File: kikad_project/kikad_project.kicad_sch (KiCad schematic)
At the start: 33 parts, among them IC1 HCPL-2531, IC2 HCPL-2531, IC3 HCPL-2531, M1 Motor_DC, M2 Motor_DC, M3 Motor_DC, M4 Stepper_Motor_bipolar, Q2 IRF5305PbF, SW1 SW_Push, U1 NRF24L01_Breakout, U10 TCST2103_MODULE, U11 DM556T, U2 STM32F103C8T6, U3 L7805, U4 L7805, U5 MD13S, U6 MD13S, U7 MD13S, U8 TCST2103_MODULE, U9 TCST2103_MODULE

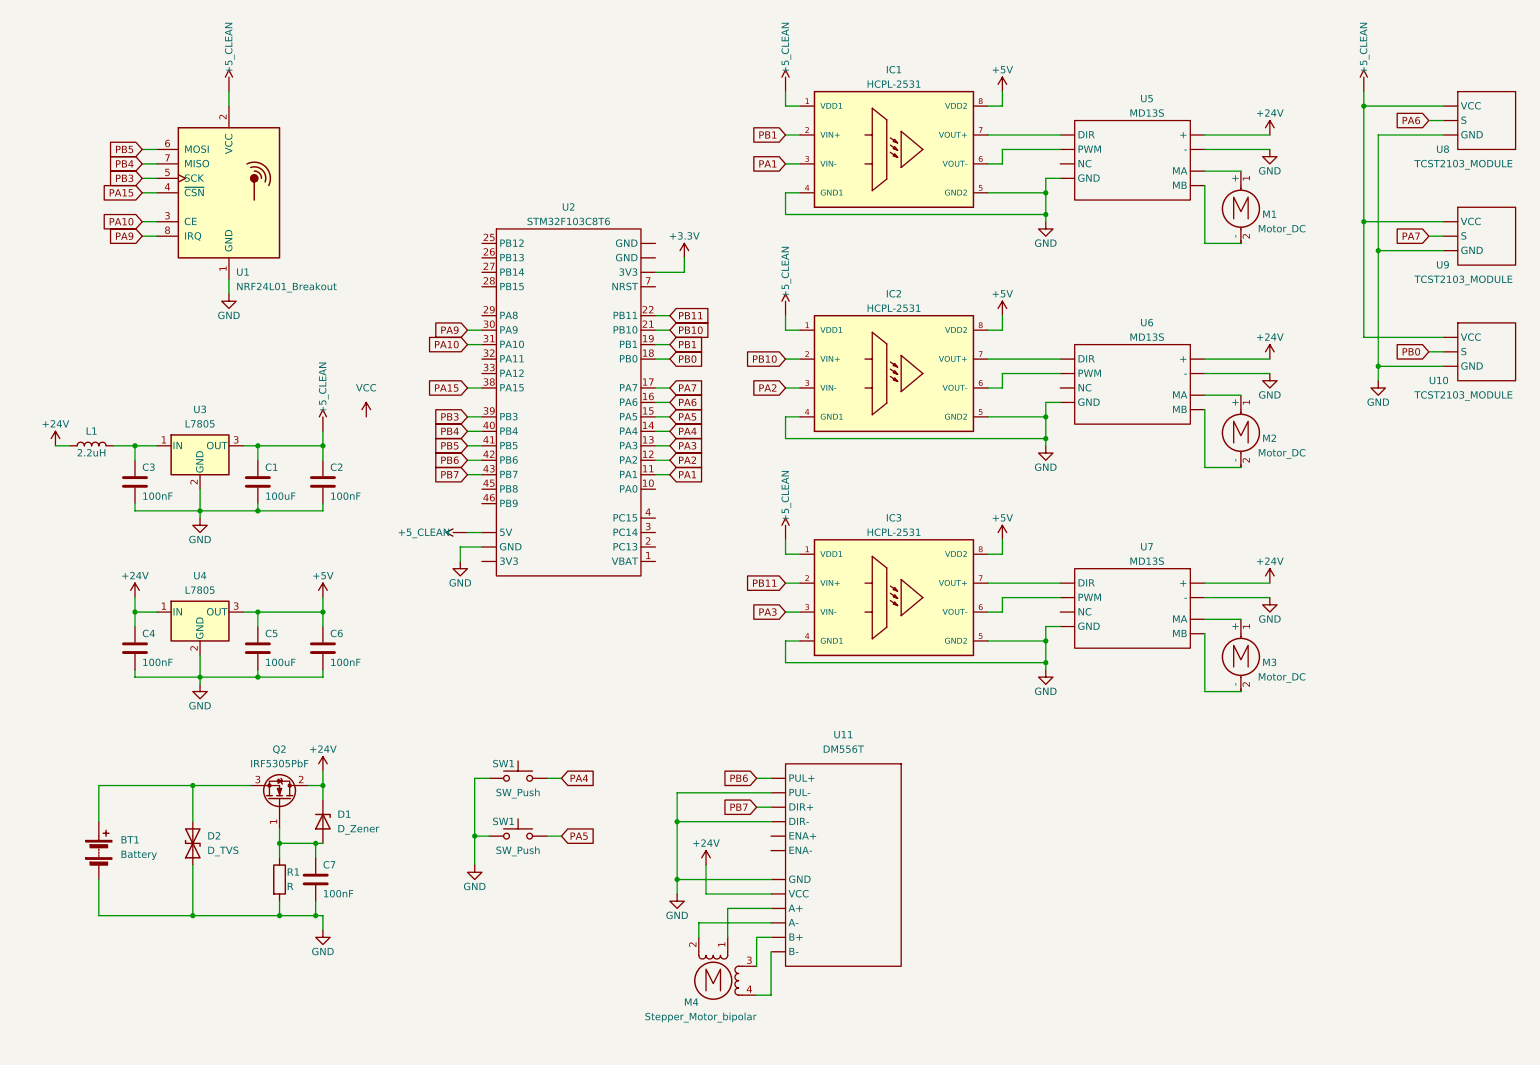
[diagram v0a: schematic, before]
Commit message: Schematics ready(excluding PCB design)
The electric schema for the PCB in the robot and the mounting schema are ready. The footprints for each element are present. However, the PCB design is not ready.
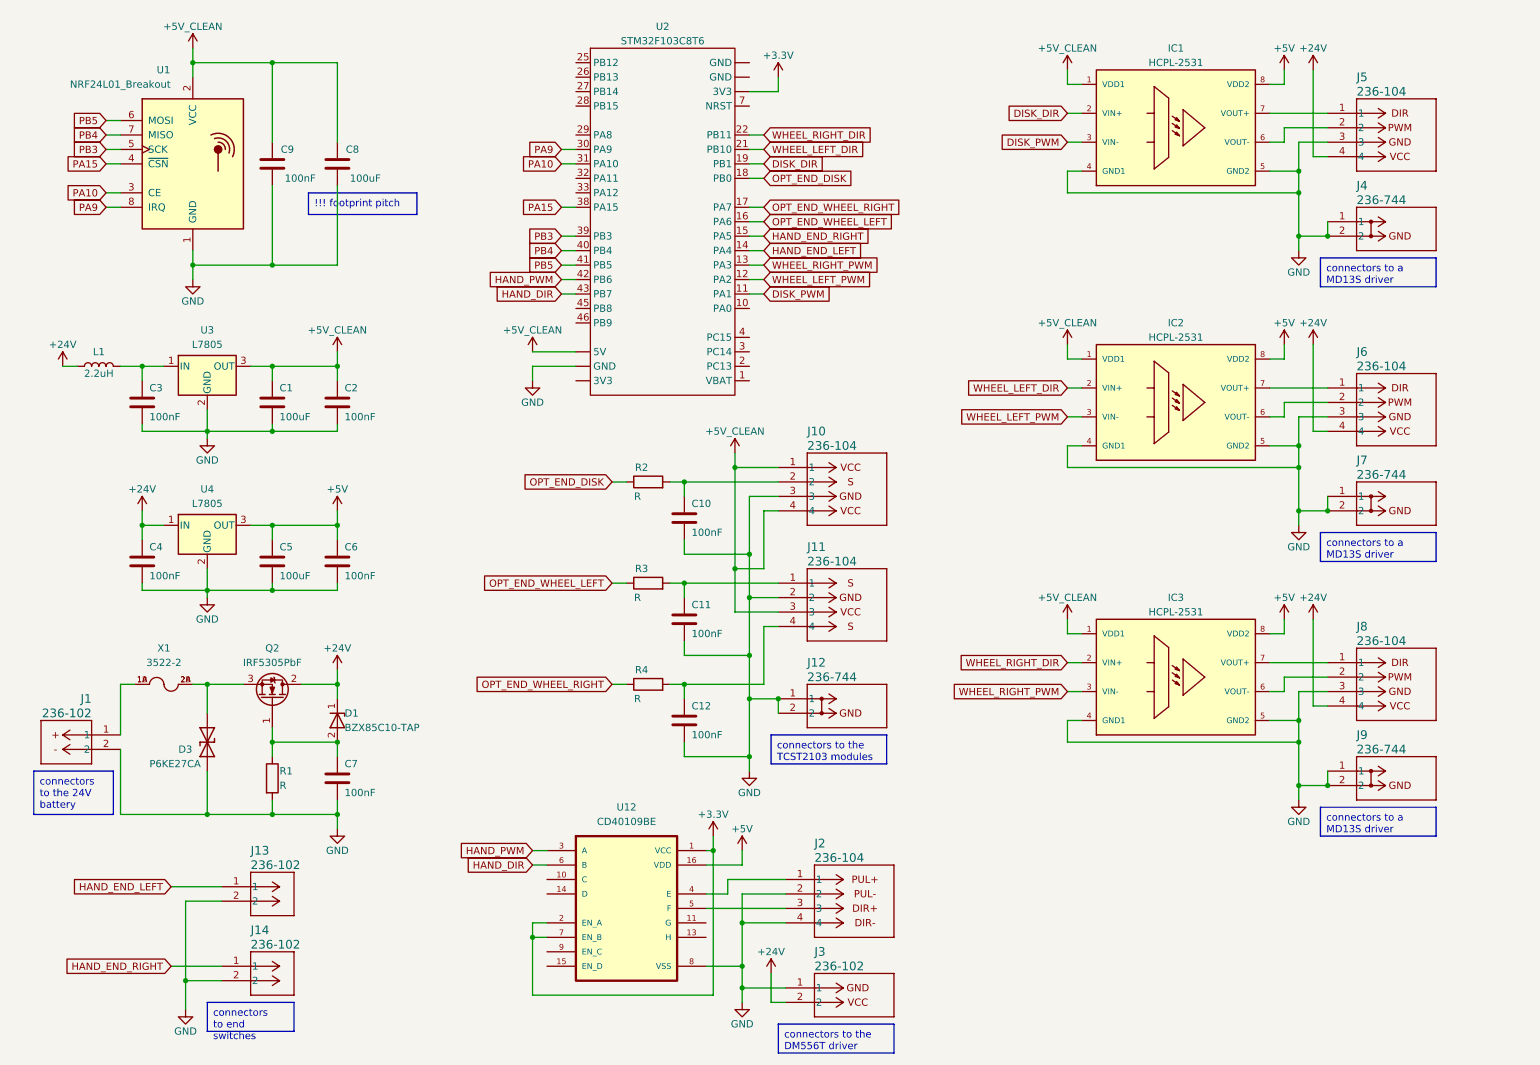
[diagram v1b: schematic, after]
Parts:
- removed BT1: Battery, symbol Device:Battery
- removed D1: D_Zener, symbol Device:D_Zener
- removed D2: D_TVS, symbol Device:D_TVS
- removed M1, M2, M3: Motor_DC, symbol Motor:Motor_DC
- removed M4: Stepper_Motor_bipolar, symbol Motor:Stepper_Motor_bipolar
- removed SW1 (x2): SW_Push, Connector_PinHeader_2.54mm:PinHeader_1x02_P2.54mm_Vertical, symbol Switch:SW_Push
- removed U10, U8, U9: TCST2103_MODULE, symbol STM32F103C8T6:TCST2103_module
- removed U11: DM556T, symbol STM32F103C8T6:DM556T
- removed U5, U6, U7: MD13S, symbol STM32F103C8T6:MD13S
- added C10, C11, C12, C9: 100nF, Capacitor_THT:C_Axial_L5.1mm_D3.1mm_P7.50mm_Horizontal, symbol Device:C
- added C8: 100uF, Capacitor_THT:CP_Radial_Tantal_D8.0mm_P2.50mm, symbol Device:C
- added D1: BZX85C10-TAP, DO-41_VIS, symbol BZX85C10-TAP:BZX85C10-TAP
- added D3: P6KE27CA, P6KE27CA:DIOAD1300W80L670D310, symbol P6KE27CA:P6KE27CA
- added J1, J13, J14, J3: 236-102, CONN_236-102_WAG, symbol 236-102:236-102
- added J10, J11, J2, J5, J6, J8: 236-104, CONN_236-104_WAG, symbol 236-104:236-104
- added J12, J4, J7, J9: 236-744, 236-744_WAG, symbol 236-744:236-744
- added R2, R3, R4: R, symbol Device:R
- added U12: CD40109BE, CD40109BE:DIP794W45P254L1969H508Q16, symbol CD40109BE:CD40109BE
- added X1: 3522-2, 3522-2:FUSE_3522-2, symbol 3522-2:3522-2
- C1, C5: footprint (none) -> Capacitor_THT:CP_Radial_Tantal_D8.0mm_P2.50mm
- C2, C3, C4, C6, C7: footprint (none) -> Capacitor_THT:C_Axial_L5.1mm_D3.1mm_P7.50mm_Horizontal
- R1: footprint (none) -> Resistor_THT:R_Axial_DIN0207_L6.3mm_D2.5mm_P10.16mm_Horizontal
- U2: footprint (none) -> Library:STM32F103C8T6_pinout
- U3, U4: footprint (none) -> Package_TO_SOT_THT:TO-220-3_Vertical
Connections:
- net +5_CLEAN is gone; now on net VCC: C1.1, C2.1, IC1.1 (VDD1), IC2.1 (VDD1), IC3.1 (VDD1), U1.2 (VCC), U2. (GND), U3.3 (OUT)
- net +24V: now also D1.1, J3.2, J5.4, J6.4, J8.4
- net +3.3V: now also U12.1 (VCC), U12.2 (EN_A), U12.7 (EN_B)
- net +5V: now also U12.16 (VDD)
- net GND: now also C10.2, C11.2, C12.2, C8.2, C9.2, D3., J1.2, J10.3, J11.2, J12.1, J12.2, J13.2, J14.2, J2.2, J2.4, J3.1, J4.1, J4.2, J5.3, J6.3, J7.1, J7.2, J8.3, J9.1, J9.2, U12.8 (VSS)
- net VCC: now also C8.1, C9.1, J10.1, J10.4, J11.3
- net at IC3.6 (VOUT-): now also J8.2
- net at IC3.7 (VOUT+): now also J8.1
- net at Q2.3 (S): now also D3., X1.2A, X1.2B
- net at IC1.6 (VOUT-): now also J5.2
- net at IC1.7 (VOUT+): now also J5.1
- net at IC2.6 (VOUT-): now also J6.2
- net at IC2.7 (VOUT+): now also J6.1
- net at C7.1, Q2.1 (G), R1.1: now also D1.2
- net PA1 renamed DISK_PWM
- net PA2 renamed WHEEL_LEFT_PWM
- net PA3 renamed WHEEL_RIGHT_PWM
- net PA4 renamed HAND_END_LEFT
- net HAND_END_LEFT: now also J13.1
- net PA5 renamed HAND_END_RIGHT
- net HAND_END_RIGHT: now also J14.1
- net PA6 renamed OPT_END_WHEEL_LEFT
- net OPT_END_WHEEL_LEFT: now also R3.1
- net PA7 renamed OPT_END_WHEEL_RIGHT
- net OPT_END_WHEEL_RIGHT: now also R4.1
- net PB0 renamed OPT_END_DISK
- net OPT_END_DISK: now also R2.1
- net PB1 renamed DISK_DIR
- net PB10 renamed WHEEL_LEFT_DIR
- net PB11 renamed WHEEL_RIGHT_DIR
- net PB6 renamed HAND_PWM
- net HAND_PWM: now also U12.3 (A)
- net PB7 renamed HAND_DIR
- net HAND_DIR: now also U12.6 (B)
- new net: J1.1, X1.1A, X1.1B
- new net: C10.1, J10.2, R2.2
- new net: J2.1, U12.4 (E)
- new net: J2.3, U12.5 (F)
- new net: C11.1, J11.1, R3.2
- new net: C12.1, J11.4, R4.2
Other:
- moved on the sheet: C1, C2, C3, C4, C5, C6, C7, IC1, L1, Q2, R1, U1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

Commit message: control upload
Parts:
- removed J4, J7, J9: 236-744, 236-744_WAG, symbol 236-744:236-744
- removed J5, J6, J8: 236-104, CONN_236-104_WAG, symbol 236-104:236-104
- added H1, H2, H3: MountingHole_Pad, MountingHole:MountingHole_3.2mm_M3_Pad, symbol Mechanical:MountingHole_Pad
- added J15, J16, J18, J4, J6, J7, J9: 236-102, 236-102:CONN_236-102_WAG, symbol 236-102:236-102
- added J17, J5, J8: 236-744, 236-744:236-744_WAG, symbol 236-744:236-744
- C1, C5, C8: footprint Capacitor_THT:CP_Radial_Tantal_D8.0mm_P2.50mm -> Capacitor_THT:CP_Radial_D5.0mm_P2.00mm
- C10, C11, C12: value 100nF -> 100uF; footprint Capacitor_THT:C_Axial_L5.1mm_D3.1mm_P7.50mm_Horizontal -> Capacitor_THT:CP_Radial_D5.0mm_P2.00mm
- D1: footprint DO-41_VIS -> BZX85C10-TAP:DO-41_VIS
- J1, J13, J14, J3: footprint CONN_236-102_WAG -> 236-102:CONN_236-102_WAG
- J10, J11, J2: footprint CONN_236-104_WAG -> 236-104:CONN_236-104_WAG
- J12: footprint 236-744_WAG -> 236-744:236-744_WAG
- L1: footprint (none) -> Inductor_THT:L_Axial_L16.0mm_D7.5mm_P5.08mm_Vertical_Fastron_XHBCC
- R1: value R -> 8.2kR
- R2, R3, R4: value R -> 6.8МR; footprint (none) -> Resistor_THT:R_Axial_DIN0207_L6.3mm_D2.5mm_P10.16mm_Horizontal
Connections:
- net +24V: now also J18.1, J6.1, J9.1
- net +3.3V: now also C8.1, C9.1, U1.2 (VCC), U2.3v (3V3); no longer U2. (GND)
- net DISK_DIR: now also IC1.3 (VIN-), U2.16 (PA6); no longer IC1.2 (VIN+), U2.19 (PB1)
- net DISK_PWM: now also IC1.2 (VIN+), U2.19 (PB1); no longer IC1.3 (VIN-), U2.11 (PA1)
- net GND: now also D3.C, U2.G (GND), H1.1, H2.1, H3.1, J17.1, J17.2, J18.2, J5.1, J5.2, J6.2, J8.1, J8.2, J9.2; no longer D3., U2. (GND)
- net HAND_DIR: now also U2.12 (PA2); no longer U2.43 (PB7)
- net HAND_END_LEFT: now also U2.29 (PA8); no longer U2.14 (PA4)
- net HAND_END_RIGHT: now also U2.28 (PB15); no longer U2.15 (PA5)
- net HAND_PWM: now also U2.11 (PA1); no longer U2.42 (PB6)
- net OPT_END_DISK: now also C10.1, U2.46 (PB9); no longer U2.18 (PB0)
- net OPT_END_WHEEL_LEFT: now also C12.1, R4.1, U2.45 (PB8); no longer R3.1, U2.16 (PA6)
- net OPT_END_WHEEL_RIGHT: now also C11.1, R3.1, U2.43 (PB7); no longer R4.1, U2.17 (PA7)
- net VCC: now also U2.5v (5V); no longer C8.1, C9.1, U1.2 (VCC), U2. (GND)
- net WHEEL_LEFT_DIR: now also IC2.3 (VIN-), U2.15 (PA5); no longer IC2.2 (VIN+), U2.21 (PB10)
- net WHEEL_LEFT_PWM: now also IC2.2 (VIN+), U2.18 (PB0); no longer IC2.3 (VIN-), U2.12 (PA2)
- net WHEEL_RIGHT_DIR: now also IC3.3 (VIN-), U2.14 (PA4); no longer IC3.2 (VIN+), U2.22 (PB11)
- net WHEEL_RIGHT_PWM: now also IC3.2 (VIN+), U2.17 (PA7); no longer IC3.3 (VIN-), U2.13 (PA3)
- net at Q2.3 (S), X1.2A, X1.2B: now also D3.A; no longer D3.
- net at IC1.6 (VOUT-): now also J4.1
- net at IC1.7 (VOUT+): now also J4.2
- net at X1.1A, X1.1B: now also J15.1; no longer J1.1
- net at IC3.7 (VOUT+): now also J16.2
- net at IC3.6 (VOUT-): now also J16.1
- net at J10.2, R2.2: no longer C10.1
- net at IC2.7 (VOUT+): now also J7.2
- net at IC2.6 (VOUT-): now also J7.1
- net at J11.1, R3.2: no longer C11.1
- net at J11.4, R4.2: no longer C12.1
- new net: J1.1, J15.2
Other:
- moved on the sheet: IC1, IC2, IC3, J1, J13, J14

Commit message: PCB ready
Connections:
- net DISK_PWM: now also U2.17 (PA7); no longer U2.19 (PB1)
- net WHEEL_RIGHT_PWM: now also U2.19 (PB1); no longer U2.17 (PA7)
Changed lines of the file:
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@@
+    )
+  )
+  (global_label "WHEEL_RIGHT_PWM" (shape input) (at 144.78 40.64 0) (fields_autoplaced)
+    (effects (font (size 1.27 1.27)) (justify left))
+    (property "Intersheetrefs" "${INTERSHEET_REFS}" (at 165.4241 40.64 0)
+      (effects (font (size 1.27 1.27)) (justify left) hide)
     )
   )
@@
     (property "Intersheetrefs" "${INTERSHEET_REFS}" (at 102.6667 38.1 0)
       (effects (font (size 1.27 1.27)) (justify right) hide)
+    )
+  )
+  (global_label "DISK_PWM" (shape input) (at 144.78 48.26 0) (fields_autoplaced)
+    (effects (font (size 1.27 1.27)) (justify left))
+    (property "Intersheetrefs" "${INTERSHEET_REFS}" (at 157.2599 48.26 0)
+      (effects (font (size 1.27 1.27)) (justify left) hide)
     )
   )
@@
     (effects (font (size 1.27 1.27)) (justify left))
     (property "Intersheetrefs" "${INTERSHEET_REFS}" (at 163.1865 53.34 0)
-      (effects (font (size 1.27 1.27)) (justify left) hide)
-    )
-  )
-  (global_label "WHEEL_RIGHT_PWM" (shape input) (at 144.78 48.26 0) (fields_autoplaced)
-    (effects (font (size 1.27 1.27)) (justify left))
-    (property "Intersheetrefs" "${INTERSHEET_REFS}" (at 165.4241 48.26 0)
       (effects (font (size 1.27 1.27)) (justify left) hide)
     )
@@
       (effects (font (size 1.27 1.27)) (justify left) hide)
     )
-  )
-  (global_label "DISK_PWM" (shape input) (at 144.78 40.64 0) (fields_autoplaced)
-    (effects (font (size 1.27 1.27)) (justify left))
-    (property "Intersheetrefs" "${INTERSHEET_REFS}" (at 157.2599 40.64 0)
-      (effects (font (size 1.27 1.27)) (justify left) hide)
-    )
